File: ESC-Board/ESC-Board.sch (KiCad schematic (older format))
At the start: 25 parts, among them J1 Molex, J2 Molex, J3 XT_60, U1 ACS780xLRTR-100U, U2 ACS780xLRTR-100U, U3 ACS780xLRTR-100U, U4 ACS780xLRTR-100U, U5 ESC:Blue_ESC, U6 ESC:Blue_ESC, U7 ESC:Blue_ESC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

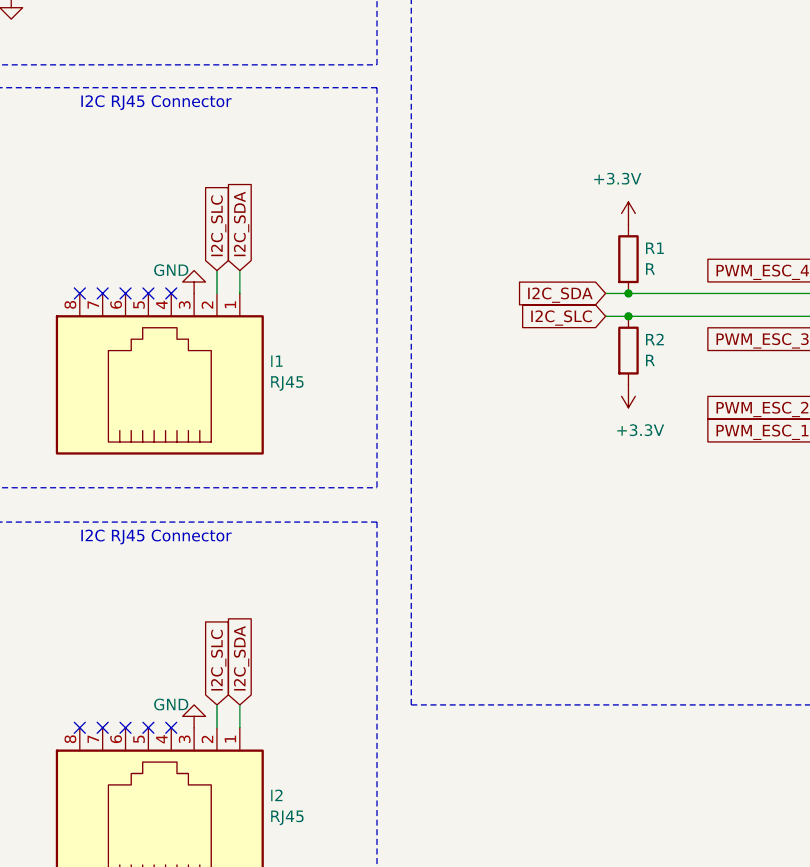
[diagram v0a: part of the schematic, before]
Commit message: Fixed issue with scl line
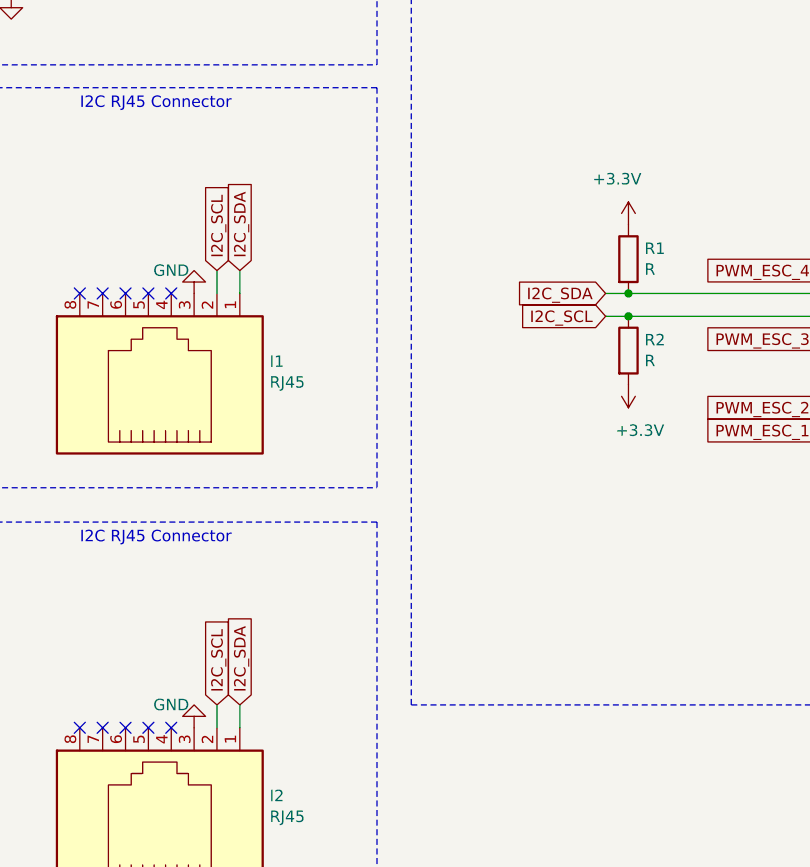
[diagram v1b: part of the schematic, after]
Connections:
- net labels added: I2C_SCL
- net labels removed: I2C_SLC
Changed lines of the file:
@@
 I2C_SDA
 Text GLabel 12500 2650 0    50   Input ~ 0
-I2C_SLC
+I2C_SCL
 Text GLabel 2050 8950 0    50   Input ~ 0
 PWM_ESC_1
@@
 Text GLabel 10900 4350 1    50   Input ~ 0
 I2C_SDA
-Text GLabel 10800 4350 1    50   Input ~ 0
-I2C_SLC
-Text GLabel 10800 2450 1    50   Input ~ 0
-I2C_SLC
 $Comp
 L power:GND #PWR0127
@@
 NoConn ~ 10500 4450
 NoConn ~ 10600 4450
+Text GLabel 10800 2450 1    50   Input ~ 0
+I2C_SCL
+Text GLabel 10800 4350 1    50   Input ~ 0
+I2C_SCL
 $EndSCHEMATC

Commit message: temp senors added not finised
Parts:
- added U10, U9: TMP235A2DBZT, TO_SOT_Packages_SMD:SOT-23, symbol ESC:TMP235A2DBZT
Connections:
- net labels added: Ext_Temp_0, Ext_Temp_1, Temp_A4, Temp_A5
- wire segments 64 -> 68
- no-connect marks 33 -> 23
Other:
- note added: "Tempure Sensors\n"
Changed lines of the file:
@@
 Wire Wire Line
 	4800 1700 4850 1700
-Text GLabel 14650 2750 2    50   Input ~ 0
+Text GLabel 14650 2950 2    50   Input ~ 0
 Current_A0
-Text GLabel 14650 2850 2    50   Input ~ 0
+Text GLabel 14650 3050 2    50   Input ~ 0
 Current_A1
-Text GLabel 14650 2950 2    50   Input ~ 0
+Text GLabel 14650 3150 2    50   Input ~ 0
 Current_A2
-Text GLabel 14650 3050 2    50   Input ~ 0
+Text GLabel 14650 3250 2    50   Input ~ 0
 Current_A3
 Wire Wire Line
@@
 NoConn ~ 1950 1900
 NoConn ~ 2050 1900
-NoConn ~ 14450 3150
-NoConn ~ 14450 3250
-NoConn ~ 14450 3350
-NoConn ~ 14450 3450
 NoConn ~ 13450 3450
 NoConn ~ 13450 3350
@@
 P 10700 2550
 F 0 "#PWR0127" H 10700 2300 50  0001 C CNN
-F 1 "GND" H 10800 2450 50  0000 C CNN
+F 1 "GND" V 10700 2350 50  0000 C CNN
 F 2 "" H 10700 2550 50  0001 C CNN
 F 3 "" H 10700 2550 50  0001 C CNN
@@
 P 10700 4450
 F 0 "#PWR0128" H 10700 4200 50  0001 C CNN
-F 1 "GND" H 10800 4350 50  0000 C CNN
+F 1 "GND" V 10700 4250 50  0000 C CNN
 F 2 "" H 10700 4450 50  0001 C CNN
 F 3 "" H 10700 4450 50  0001 C CNN
@@
 NoConn ~ 10200 2550
 NoConn ~ 10300 2550
-NoConn ~ 10400 2550
-NoConn ~ 10500 2550
-NoConn ~ 10600 2550
 NoConn ~ 10200 4450
 NoConn ~ 10300 4450
-NoConn ~ 10400 4450
-NoConn ~ 10500 4450
-NoConn ~ 10600 4450
 Text GLabel 10800 2450 1    50   Input ~ 0
 I2C_SCL
 Text GLabel 10800 4350 1    50   Input ~ 0
 I2C_SCL
+$Comp
+L ESC:TMP235A2DBZT U10
+U 1 1 5C32D7CE
+P 7750 3550
+F 0 "U10" H 7750 3250 50  0000 C CNN
+F 1 "TMP235A2DBZT" H 7725 3874 50  0000 C CNN
+F 2 "TO_SOT_Packages_SMD:SOT-23" H 7950 3600 50  0001 C CNN
+F 3 "" H 7950 3600 50  0001 C CNN
+	1    7750 3550
+	1    0    0    -1
+$EndComp
+Text GLabel 14650 2850 2    50   Input ~ 0
+Temp_A4
+Text GLabel 14650 2750 2    50   Input ~ 0
+Temp_A5
+Wire Wire Line
+	14450 3150 14650 3150
+Wire Wire Line
+	14450 3250 14650 3250
+Text GLabel 6600 3550 2    50   Input ~ 0
+Temp_A4
+Text GLabel 8150 3550 2    50   Input ~ 0
+Temp_A5
+$Comp
+L power:+3.3V #PWR0130
+U 1 1 5C33521D
+P 5750 3400
+F 0 "#PWR0130" H 5750 3250 50  0001 C CNN
+F 1 "+3.3V" V 5750 3650 50  0000 C CNN
+F 2 "" H 5750 3400 50  0001 C CNN
+F 3 "" H 5750 3400 50  0001 C CNN
+	1    5750 3400
+	0    -1   -1   0
+$EndComp
+$Comp
+L power:+3.3V #PWR0135
+U 1 1 5C3355CF
+P 7300 3400
+F 0 "#PWR0135" H 7300 3250 50  0001 C CNN
+F 1 "+3.3V" V 7300 3650 50  0000 C CNN
+F 2 "" H 7300 3400 50  0001 C CNN
+F 3 "" H 7300 3400 50  0001 C CNN
+	1    7300 3400
+	0    -1   -1   0
+$EndComp
+$Comp
+L ESC:TMP235A2DBZT U9
+U 1 1 5C336CCF
+P 6200 3550
+F 0 "U9" H 6200 3250 50  0000 C CNN
+F 1 "TMP235A2DBZT" H 6175 3874 50  0000 C CNN
+F 2 "TO_SOT_Packages_SMD:SOT-23" H 6400 3600 50  0001 C CNN
+F 3 "" H 6400 3600 50  0001 C CNN
+	1    6200 3550
+	1    0    0    -1
+$EndComp
+$Comp
+L power:GND #PWR0136
+U 1 1 5C337119
+P 5750 3700
+F 0 "#PWR0136" H 5750 3450 50  0001 C CNN
+F 1 "GND" V 5750 3500 50  0000 C CNN
+F 2 "" H 5750 3700 50  0001 C CNN
+F 3 "" H 5750 3700 50  0001 C CNN
+	1    5750 3700
+	0    1    1    0
+$EndComp
+$Comp
+L power:GND #PWR0137
+U 1 1 5C337641
+P 7300 3700
+F 0 "#PWR0137" H 7300 3450 50  0001 C CNN
+F 1 "GND" V 7300 3500 50  0000 C CNN
+F 2 "" H 7300 3700 50  0001 C CNN
+F 3 "" H 7300 3700 50  0001 C CNN
+	1    7300 3700
+	0    1    1    0
+$EndComp
+Wire Notes Line
+	5350 4050 8600 4050
+Wire Notes Line
+	8600 4050 8600 2950
+Wire Notes Line
+	8600 2950 5350 2950
+Wire Notes Line
+	5350 2950 5350 4050
+Text Notes 6650 3050 0    50   ~ 0
+Tempure Sensors\n
+$Comp
+L power:+3.3V #PWR0138
+U 1 1 5C33FC96
+P 10600 4450
+F 0 "#PWR0138" H 10600 4300 50  0001 C CNN
+F 1 "+3.3V" V 10600 4700 50  0000 C CNN
+F 2 "" H 10600 4450 50  0001 C CNN
+F 3 "" H 10600 4450 50  0001 C CNN
+	1    10600 4450
+	1    0    0    -1
+$EndComp
+$Comp
+L power:+3.3V #PWR0139
+U 1 1 5C33FE21
+P 10600 2550
+F 0 "#PWR0139" H 10600 2400 50  0001 C CNN
+F 1 "+3.3V" V 10600 2800 50  0000 C CNN
+F 2 "" H 10600 2550 50  0001 C CNN
+F 3 "" H 10600 2550 50  0001 C CNN
+	1    10600 2550
+	1    0    0    -1
+$EndComp
+Text GLabel 10500 4450 1    50   Input ~ 0
+Ext_Temp_0
+Text GLabel 10400 4450 1    50   Input ~ 0
+Ext_Temp_1
+Text GLabel 10500 2550 1    50   Input ~ 0
+Ext_Temp_0
+Text GLabel 10400 2550 1    50   Input ~ 0
+Ext_Temp_1
+Text GLabel 14650 3450 2    50   Input ~ 0
+Ext_Temp_0
+Text GLabel 14650 3350 2    50   Input ~ 0
+Ext_Temp_1
+Wire Wire Line
+	14650 3350 14450 3350
+Wire Wire Line
+	14650 3450 14450 3450
 $EndSCHEMATC

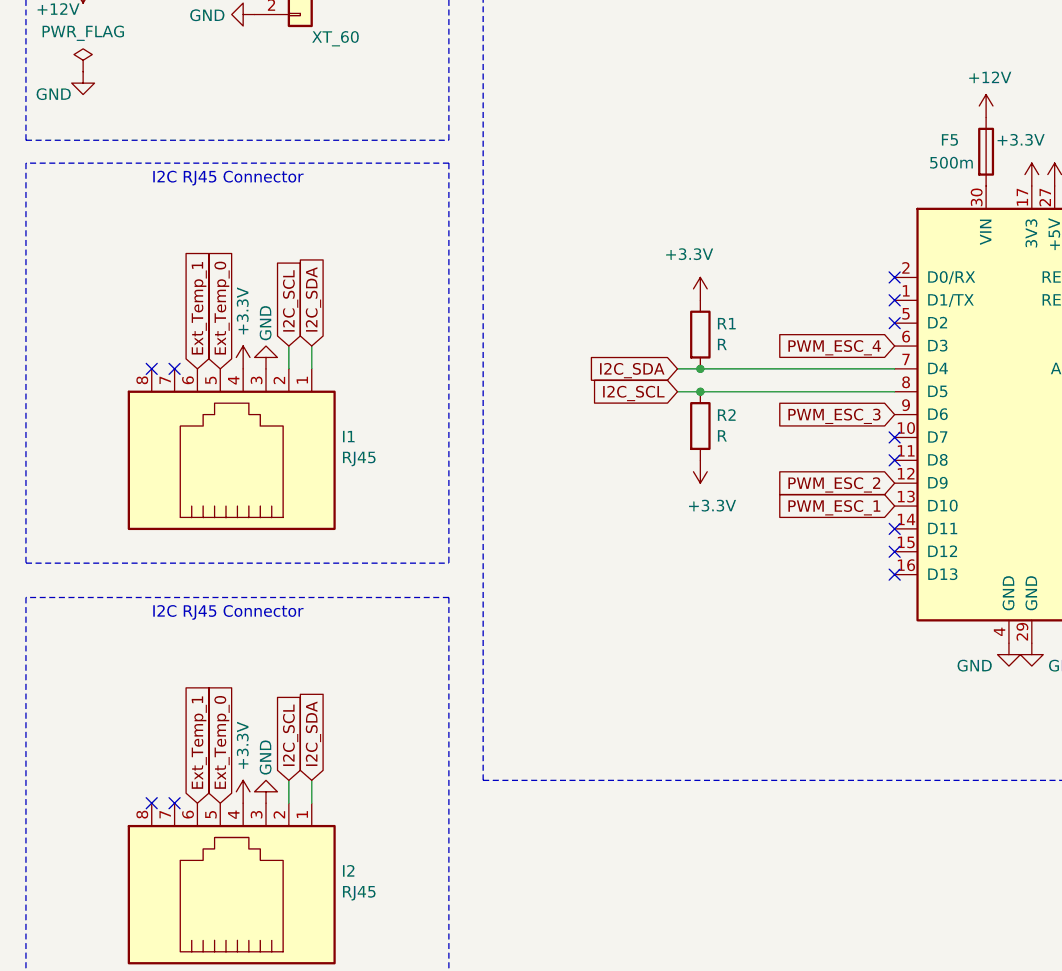
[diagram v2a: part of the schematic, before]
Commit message: Updated PDU and ESC for leak sensor
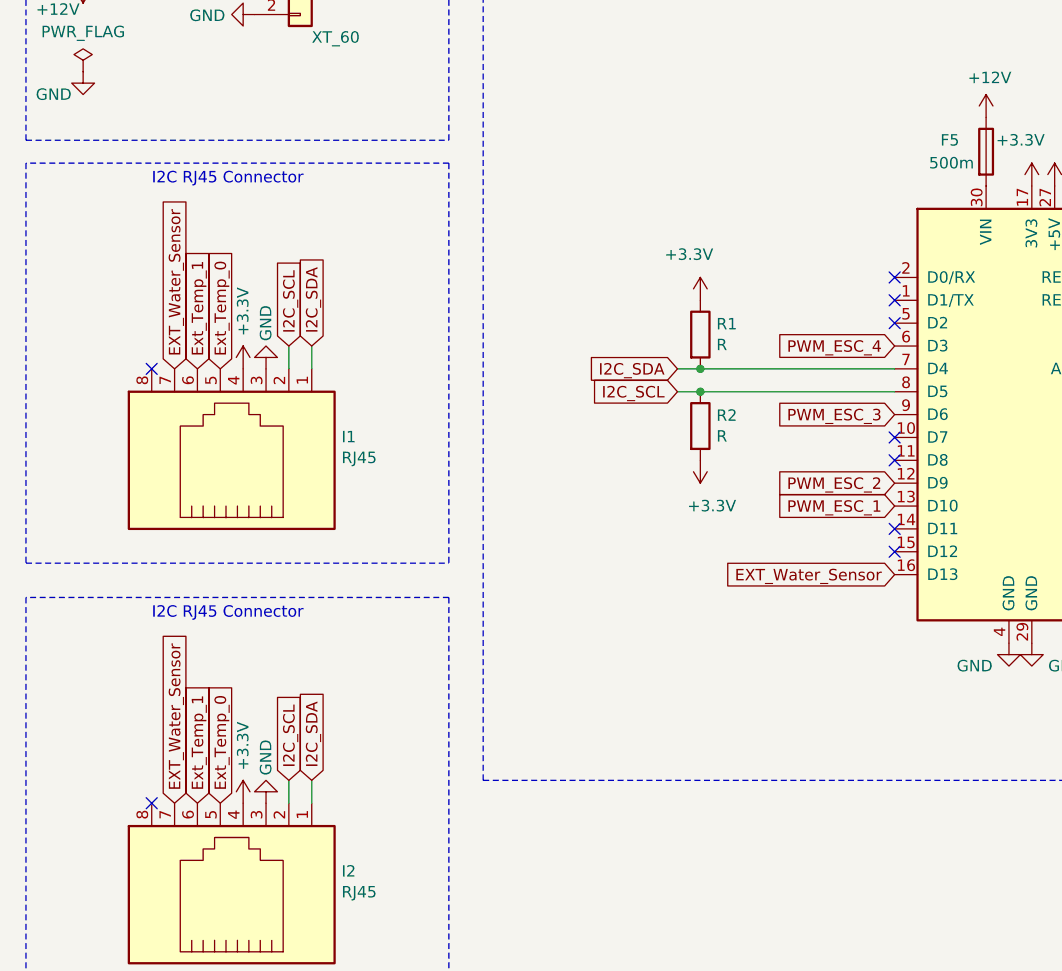
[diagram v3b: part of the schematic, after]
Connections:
- net labels added: EXT_Water_Sensor
- no-connect marks 23 -> 20
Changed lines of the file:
@@
 NoConn ~ 1950 1900
 NoConn ~ 2050 1900
-NoConn ~ 13450 3450
 NoConn ~ 13450 3350
 NoConn ~ 13450 3250
@@
 $EndComp
 NoConn ~ 10200 2550
-NoConn ~ 10300 2550
 NoConn ~ 10200 4450
-NoConn ~ 10300 4450
 Text GLabel 10800 2450 1    50   Input ~ 0
 I2C_SCL
@@
 Wire Wire Line
 	14650 3450 14450 3450
+Text GLabel 10300 4450 1    50   Input ~ 0
+EXT_Water_Sensor
+Text GLabel 10300 2550 1    50   Input ~ 0
+EXT_Water_Sensor
+Text GLabel 13450 3450 0    50   Input ~ 0
+EXT_Water_Sensor
 $EndSCHEMATC

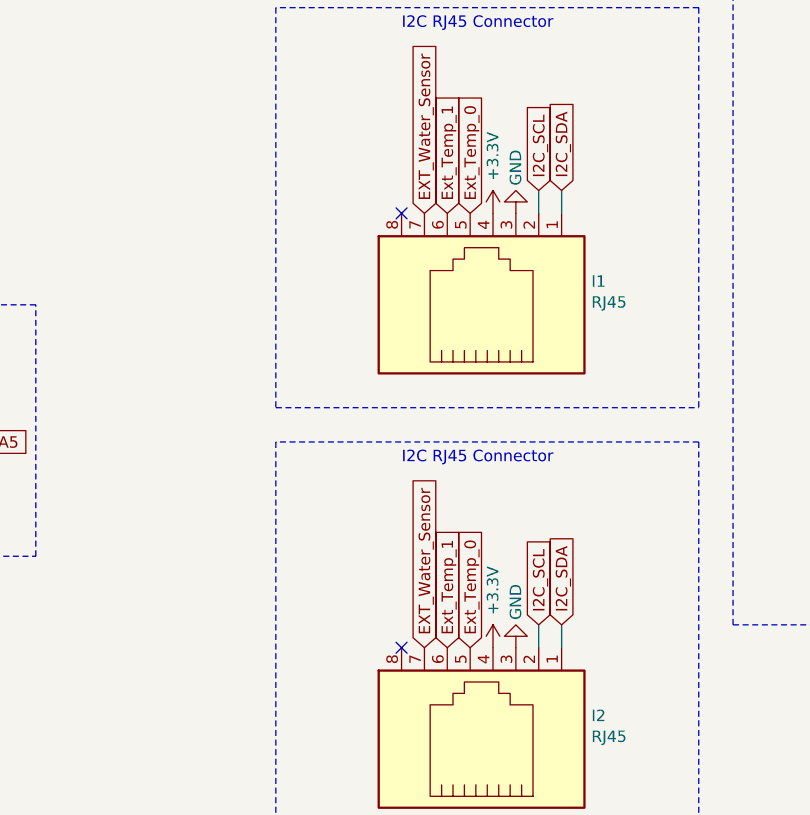
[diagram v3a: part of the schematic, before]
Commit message: Added 5v
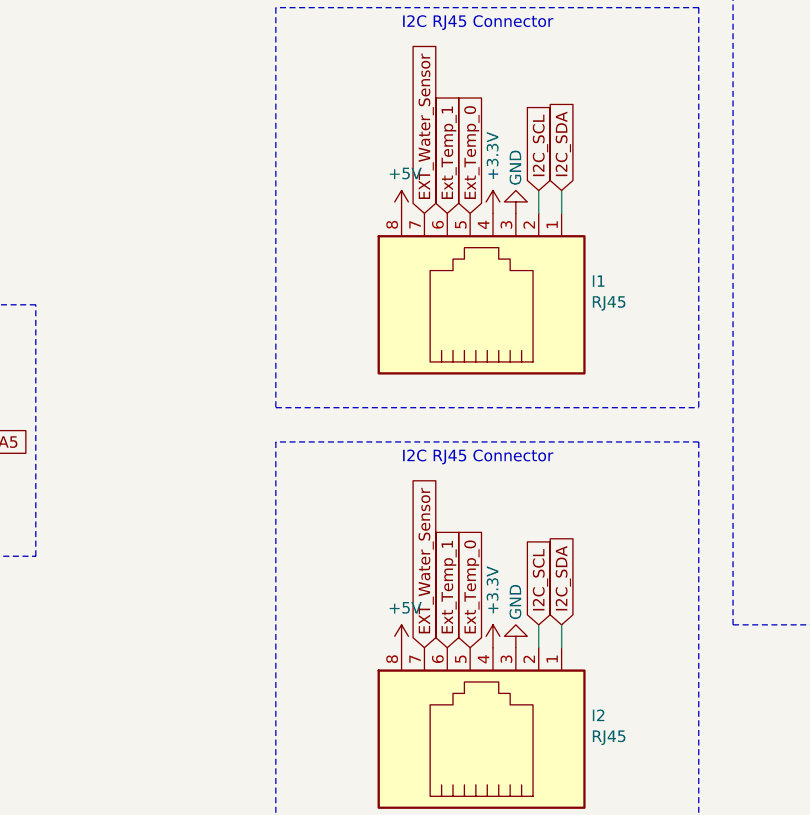
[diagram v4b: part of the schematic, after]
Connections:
- no-connect marks 20 -> 18
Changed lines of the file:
@@
 	-1   0    0    1
 $EndComp
-NoConn ~ 10200 2550
-NoConn ~ 10200 4450
 Text GLabel 10800 2450 1    50   Input ~ 0
 I2C_SCL
@@
 Text GLabel 13450 3450 0    50   Input ~ 0
 EXT_Water_Sensor
+$Comp
+L power:+5V #PWR?
+U 1 1 5C5A7FFD
+P 10200 4450
+F 0 "#PWR?" H 10200 4300 50  0001 C CNN
+F 1 "+5V" H 10215 4623 50  0000 C CNN
+F 2 "" H 10200 4450 50  0001 C CNN
+F 3 "" H 10200 4450 50  0001 C CNN
+	1    10200 4450
+	1    0    0    -1
+$EndComp
+$Comp
+L power:+5V #PWR?
+U 1 1 5C5A8045
+P 10200 2550
+F 0 "#PWR?" H 10200 2400 50  0001 C CNN
+F 1 "+5V" H 10215 2723 50  0000 C CNN
+F 2 "" H 10200 2550 50  0001 C CNN
+F 3 "" H 10200 2550 50  0001 C CNN
+	1    10200 2550
+	1    0    0    -1
+$EndComp
 $EndSCHEMATC

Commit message: Finalized
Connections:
- net labels added: EXT_PWM_LED
- net labels removed: EXT_Water_Sensor
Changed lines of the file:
@@
 NoConn ~ 2050 1900
 NoConn ~ 13450 3350
-NoConn ~ 13450 3250
 NoConn ~ 13450 2950
 NoConn ~ 13450 2850
@@
 Wire Wire Line
 	14650 3450 14450 3450
-Text GLabel 10300 4450 1    50   Input ~ 0
-EXT_Water_Sensor
-Text GLabel 10300 2550 1    50   Input ~ 0
-EXT_Water_Sensor
-Text GLabel 13450 3450 0    50   Input ~ 0
-EXT_Water_Sensor
 $Comp
 L power:+5V #PWR?
@@
 	1    0    0    -1
 $EndComp
+Text GLabel 13450 3250 0    50   Input ~ 0
+EXT_PWM_LED
+NoConn ~ 13450 3450
+Text GLabel 10300 2550 1    50   Input ~ 0
+EXT_PWM_LED
+Text GLabel 10300 4450 1    50   Input ~ 0
+EXT_PWM_LED
 $EndSCHEMATC
